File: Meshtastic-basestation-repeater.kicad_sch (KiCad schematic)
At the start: 8 parts, among them J1 DC IN, J2 GPS voltage, J3 GPS, U1 LM1084-5.0, U2 AMS1117-3.3, U3 ESP32-S3-WROOM-1U, U4 E22-900M30S

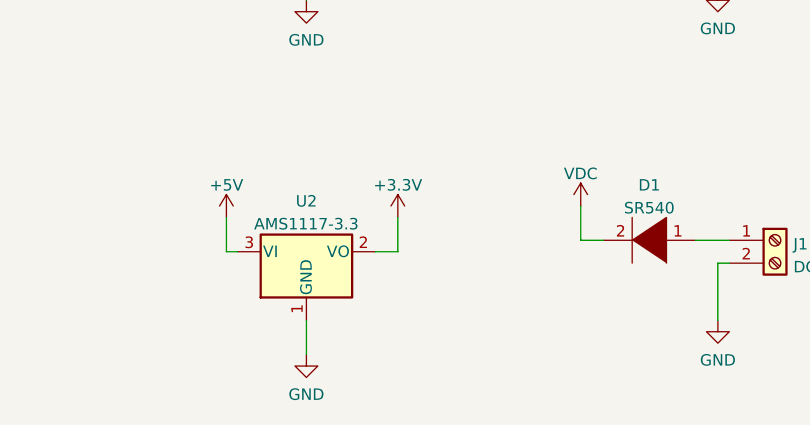
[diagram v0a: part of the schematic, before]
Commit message: Added 1N5361 zener as TSD
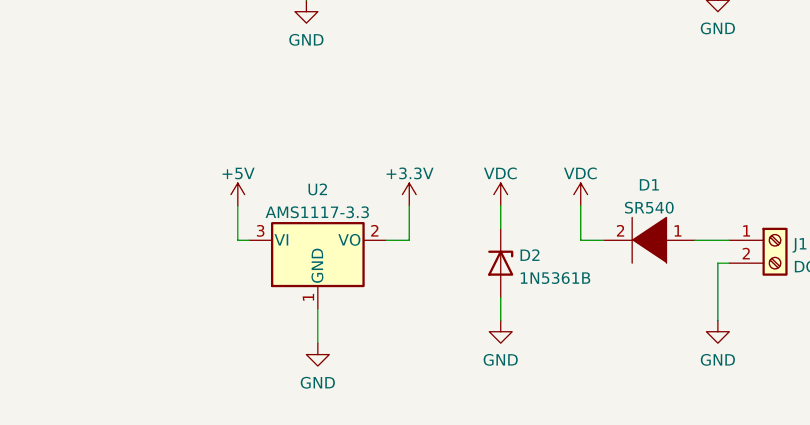
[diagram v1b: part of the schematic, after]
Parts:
- added D2: 1N5361B, Diode_THT:D_DO-201_P15.24mm_Horizontal, symbol Diode:1N53xxB
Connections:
- net GND: now also D2.2 (A)
- net VDC: now also D2.1 (K)
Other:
- moved on the sheet: U2
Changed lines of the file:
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@@
     (comment 4 "WIP - NOT READY")
   )
+  (wire (pts (xy 228.6 142.24) (xy 228.6 144.78))
+    (stroke (width 0) (type default) (color 0 0 0 0))
+  )
   (wire (pts (xy 207.01 106.68) (xy 207.01 109.22))
     (stroke (width 0) (type default) (color 0 0 0 0))
@@
     (stroke (width 0) (type default) (color 0 0 0 0))
   )
-  (wire (pts (xy 217.17 137.16) (xy 214.63 137.16))
+  (wire (pts (xy 218.44 135.89) (xy 215.9 135.89))
     (stroke (width 0) (type default) (color 0 0 0 0))
   )
@@
     (stroke (width 0) (type default) (color 0 0 0 0))
   )
-  (wire (pts (xy 198.12 133.35) (xy 198.12 137.16))
-    (stroke (width 0) (type default) (color 0 0 0 0))
-  )
-  (wire (pts (xy 198.12 137.16) (xy 199.39 137.16))
+  (wire (pts (xy 199.39 132.08) (xy 199.39 135.89))
+    (stroke (width 0) (type default) (color 0 0 0 0))
+  )
+  (wire (pts (xy 199.39 135.89) (xy 200.66 135.89))
     (stroke (width 0) (type default) (color 0 0 0 0))
   )
@@
     (stroke (width 0) (type default) (color 0 0 0 0))
   )
-  (wire (pts (xy 217.17 133.35) (xy 217.17 137.16))
-    (stroke (width 0) (type default) (color 0 0 0 0))
-  )
-  (wire (pts (xy 207.01 144.78) (xy 207.01 148.59))
+  (wire (pts (xy 218.44 132.08) (xy 218.44 135.89))
+    (stroke (width 0) (type default) (color 0 0 0 0))
+  )
+  (wire (pts (xy 208.28 143.51) (xy 208.28 147.32))
     (stroke (width 0) (type default) (color 0 0 0 0))
   )
@@
   )
   (wire (pts (xy 196.85 95.25) (xy 196.85 99.06))
+    (stroke (width 0) (type default) (color 0 0 0 0))
+  )
+  (wire (pts (xy 228.6 132.08) (xy 228.6 134.62))
     (stroke (width 0) (type default) (color 0 0 0 0))
   )
@@
     (pin "2")
     (pin "3")
+  )
+  (symbol (lib_id "power:VDC") (at 228.6 132.08 0) (unit 1)
+    (in_bom yes) (on_board yes) (fields_autoplaced)
+    (property "Reference" "#PWR?" (id 0) (at 228.6 134.62 0)
+      (effects (font (size 1.27 1.27)) hide)
+    )
+    (property "Value" "VDC" (id 1) (at 228.6 128.5042 0))
+    (property "Footprint" "" (id 2) (at 228.6 132.08 0)
+      (effects (font (size 1.27 1.27)) hide)
+    )
+    (property "Datasheet" "" (id 3) (at 228.6 132.08 0)
+      (effects (font (size 1.27 1.27)) hide)
+    )
+    (pin "1")
+  )
+  (symbol (lib_id "Diode:1N53xxB") (at 228.6 138.43 270) (unit 1)
+    (in_bom yes) (on_board yes) (fields_autoplaced)
+    (property "Reference" "D2" (id 0) (at 230.632 137.5953 90)
+      (effects (font (size 1.27 1.27)) (justify left))
+    )
+    (property "Value" "1N5361B" (id 1) (at 230.632 140.1322 90)
+      (effects (font (size 1.27 1.27)) (justify left))
+    )
+    (property "Footprint" "Diode_THT:D_DO-201_P15.24mm_Horizontal" (id 2) (at 224.155 138.43 0)
+      (effects (font (size 1.27 1.27)) hide)
+    )
+    (property "Datasheet" "https://diotec.com/tl_files/diotec/files/pdf/datasheets/1n5345b.pdf" (id 3) (at 228.6 138.43 0)
+      (effects (font (size 1.27 1.27)) hide)
+    )
+    (pin "1")
+    (pin "2")
   )
   (symbol (lib_id "power:+3.3V") (at 229.87 91.44 0) (unit 1)
@@
     (pin "9")
   )
-  (symbol (lib_id "power:+5V") (at 198.12 133.35 0) (unit 1)
-    (in_bom yes) (on_board yes) (fields_autoplaced)
-    (property "Reference" "#PWR?" (id 0) (at 198.12 137.16 0)
-      (effects (font (size 1.27 1.27)) hide)
-    )
-    (property "Value" "+5V" (id 1) (at 198.12 129.7742 0))
-    (property "Footprint" "" (id 2) (at 198.12 133.35 0)
-      (effects (font (size 1.27 1.27)) hide)
-    )
-    (property "Datasheet" "" (id 3) (at 198.12 133.35 0)
+  (symbol (lib_id "power:+5V") (at 199.39 132.08 0) (unit 1)
+    (in_bom yes) (on_board yes) (fields_autoplaced)
+    (property "Reference" "#PWR?" (id 0) (at 199.39 135.89 0)
+      (effects (font (size 1.27 1.27)) hide)
+    )
+    (property "Value" "+5V" (id 1) (at 199.39 128.5042 0))
+    (property "Footprint" "" (id 2) (at 199.39 132.08 0)
+      (effects (font (size 1.27 1.27)) hide)
+    )
+    (property "Datasheet" "" (id 3) (at 199.39 132.08 0)
       (effects (font (size 1.27 1.27)) hide)
     )
@@
     (pin "1")
   )
-  (symbol (lib_id "Regulator_Linear:AMS1117-3.3") (at 207.01 137.16 0) (unit 1)
-    (in_bom yes) (on_board yes) (fields_autoplaced)
-    (property "Reference" "U2" (id 0) (at 207.01 131.5552 0))
-    (property "Value" "AMS1117-3.3" (id 1) (at 207.01 134.0921 0))
-    (property "Footprint" "Package_TO_SOT_SMD:SOT-223-3_TabPin2" (id 2) (at 207.01 132.08 0)
-      (effects (font (size 1.27 1.27)) hide)
-    )
-    (property "Datasheet" "http://www.advanced-monolithic.com/pdf/ds1117.pdf" (id 3) (at 209.55 143.51 0)
+  (symbol (lib_id "Regulator_Linear:AMS1117-3.3") (at 208.28 135.89 0) (unit 1)
+    (in_bom yes) (on_board yes) (fields_autoplaced)
+    (property "Reference" "U2" (id 0) (at 208.28 130.2852 0))
+    (property "Value" "AMS1117-3.3" (id 1) (at 208.28 132.8221 0))
+    (property "Footprint" "Package_TO_SOT_SMD:SOT-223-3_TabPin2" (id 2) (at 208.28 130.81 0)
+      (effects (font (size 1.27 1.27)) hide)
+    )
+    (property "Datasheet" "http://www.advanced-monolithic.com/pdf/ds1117.pdf" (id 3) (at 210.82 142.24 0)
       (effects (font (size 1.27 1.27)) hide)
     )
@@
     (pin "3")
   )
-  (symbol (lib_id "power:+3.3V") (at 217.17 133.35 0) (unit 1)
-    (in_bom yes) (on_board yes) (fields_autoplaced)
-    (property "Reference" "#PWR?" (id 0) (at 217.17 137.16 0)
-      (effects (font (size 1.27 1.27)) hide)
-    )
-    (property "Value" "+3.3V" (id 1) (at 217.17 129.7742 0))
-    (property "Footprint" "" (id 2) (at 217.17 133.35 0)
-      (effects (font (size 1.27 1.27)) hide)
-    )
-    (property "Datasheet" "" (id 3) (at 217.17 133.35 0)
+  (symbol (lib_id "power:+3.3V") (at 218.44 132.08 0) (unit 1)
+    (in_bom yes) (on_board yes) (fields_autoplaced)
+    (property "Reference" "#PWR?" (id 0) (at 218.44 135.89 0)
+      (effects (font (size 1.27 1.27)) hide)
+    )
+    (property "Value" "+3.3V" (id 1) (at 218.44 128.5042 0))
+    (property "Footprint" "" (id 2) (at 218.44 132.08 0)
+      (effects (font (size 1.27 1.27)) hide)
+    )
+    (property "Datasheet" "" (id 3) (at 218.44 132.08 0)
       (effects (font (size 1.27 1.27)) hide)
     )
@@
     (pin "2")
   )
-  (symbol (lib_id "power:GND") (at 207.01 148.59 0) (unit 1)
-    (in_bom yes) (on_board yes) (fields_autoplaced)
-    (property "Reference" "#PWR?" (id 0) (at 207.01 154.94 0)
-      (effects (font (size 1.27 1.27)) hide)
-    )
-    (property "Value" "GND" (id 1) (at 207.01 153.0334 0))
-    (property "Footprint" "" (id 2) (at 207.01 148.59 0)
-      (effects (font (size 1.27 1.27)) hide)
-    )
-    (property "Datasheet" "" (id 3) (at 207.01 148.59 0)
+  (symbol (lib_id "power:GND") (at 208.28 147.32 0) (unit 1)
+    (in_bom yes) (on_board yes) (fields_autoplaced)
+    (property "Reference" "#PWR?" (id 0) (at 208.28 153.67 0)
+      (effects (font (size 1.27 1.27)) hide)
+    )
+    (property "Value" "GND" (id 1) (at 208.28 151.7634 0))
+    (property "Footprint" "" (id 2) (at 208.28 147.32 0)
+      (effects (font (size 1.27 1.27)) hide)
+    )
+    (property "Datasheet" "" (id 3) (at 208.28 147.32 0)
       (effects (font (size 1.27 1.27)) hide)
     )
@@
     (pin "9")
   )
+  (symbol (lib_id "power:GND") (at 228.6 144.78 0) (unit 1)
+    (in_bom yes) (on_board yes) (fields_autoplaced)
+    (property "Reference" "#PWR?" (id 0) (at 228.6 151.13 0)
+      (effects (font (size 1.27 1.27)) hide)
+    )
+    (property "Value" "GND" (id 1) (at 228.6 149.2234 0))
+    (property "Footprint" "" (id 2) (at 228.6 144.78 0)
+      (effects (font (size 1.27 1.27)) hide)
+    )
+    (property "Datasheet" "" (id 3) (at 228.6 144.78 0)
+      (effects (font (size 1.27 1.27)) hide)
+    )
+    (pin "1")
+  )
   (sheet_instances
     (path "/" (page "1"))
   )
   (symbol_instances
+    (path "/050bdd80-6230-424a-ab22-b0ebe32c2b09"
+      (reference "#PWR?") (unit 1) (value "VDC") (footprint "")
+    )
     (path "/14aedd38-96b1-44f3-a46a-1991abd80956"
       (reference "#PWR?") (unit 1) (value "+3.3V") (footprint "")
@@
       (reference "#PWR?") (unit 1) (value "VDC") (footprint "")
     )
+    (path "/f3549e33-105d-4e2b-a396-27200e369bbe"
+      (reference "#PWR?") (unit 1) (value "GND") (footprint "")
+    )
     (path "/d1c663d1-bac6-47fc-a77e-ea137b1500ea"
       (reference "D1") (unit 1) (value "SR540") (footprint "")
     )
+    (path "/0da9fe8b-c069-4698-807a-05a52047b222"
+      (reference "D2") (unit 1) (value "1N5361B") (footprint "Diode_THT:D_DO-201_P15.24mm_Horizontal")
+    )
     (path "/adc0169a-affa-4b53-8b54-b96780474997"
